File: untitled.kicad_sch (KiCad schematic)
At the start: 18 parts, among them J1 Conn_01x08_Female, J2 Conn_01x08_Female, J3 Conn_01x03_Female, J5 Conn_01x03_Female, J6 Conn_01x03_Female

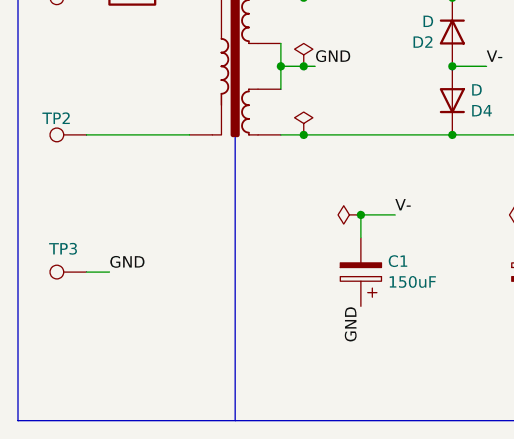
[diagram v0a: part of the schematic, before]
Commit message: sorting out earths and making measure mux board
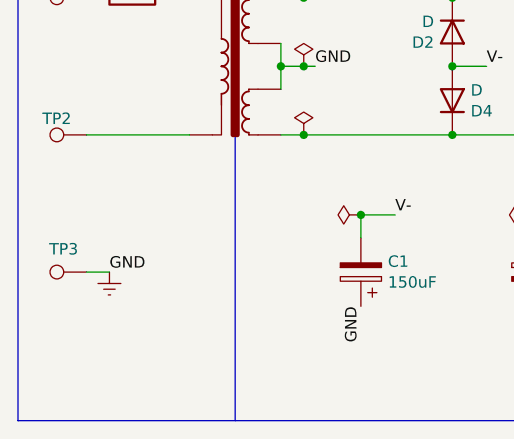
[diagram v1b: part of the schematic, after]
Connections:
- net GND renamed Earth
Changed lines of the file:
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@@
     (pin "2")
+  )
+  (symbol (lib_id "power:Earth") (at 74.676 114.046 0) (unit 1)
+    (in_bom yes) (on_board yes) (fields_autoplaced)
+    (property "Reference" "#PWR0105" (id 0) (at 74.676 120.396 0)
+      (effects (font (size 1.27 1.27)) hide)
+    )
+    (property "Value" "Earth" (id 1) (at 74.676 117.856 0)
+      (effects (font (size 1.27 1.27)) hide)
+    )
+    (property "Footprint" "" (id 2) (at 74.676 114.046 0)
+      (effects (font (size 1.27 1.27)) hide)
+    )
+    (property "Datasheet" "~" (id 3) (at 74.676 114.046 0)
+      (effects (font (size 1.27 1.27)) hide)
+    )
+    (pin "1")
   )
   (symbol (lib_id "Connector:TestPoint") (at 72.136 83.566 90) (unit 1)
